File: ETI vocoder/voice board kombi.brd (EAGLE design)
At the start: 160 x 100 mm, 169 parts, among them IC1 TL072P, IC1. TL072P, IC2 TL072P, IC2. TL072P, IC3 TL081P, IC3. TL081P, IC4 TL081P, IC4. TL081P, IC5 TL072P, IC6 LM13600AN, IC7 TL072P, IC7. TL072P, Q1 BF244, Q1. BF244, Q2 BC214, Q2. BC214

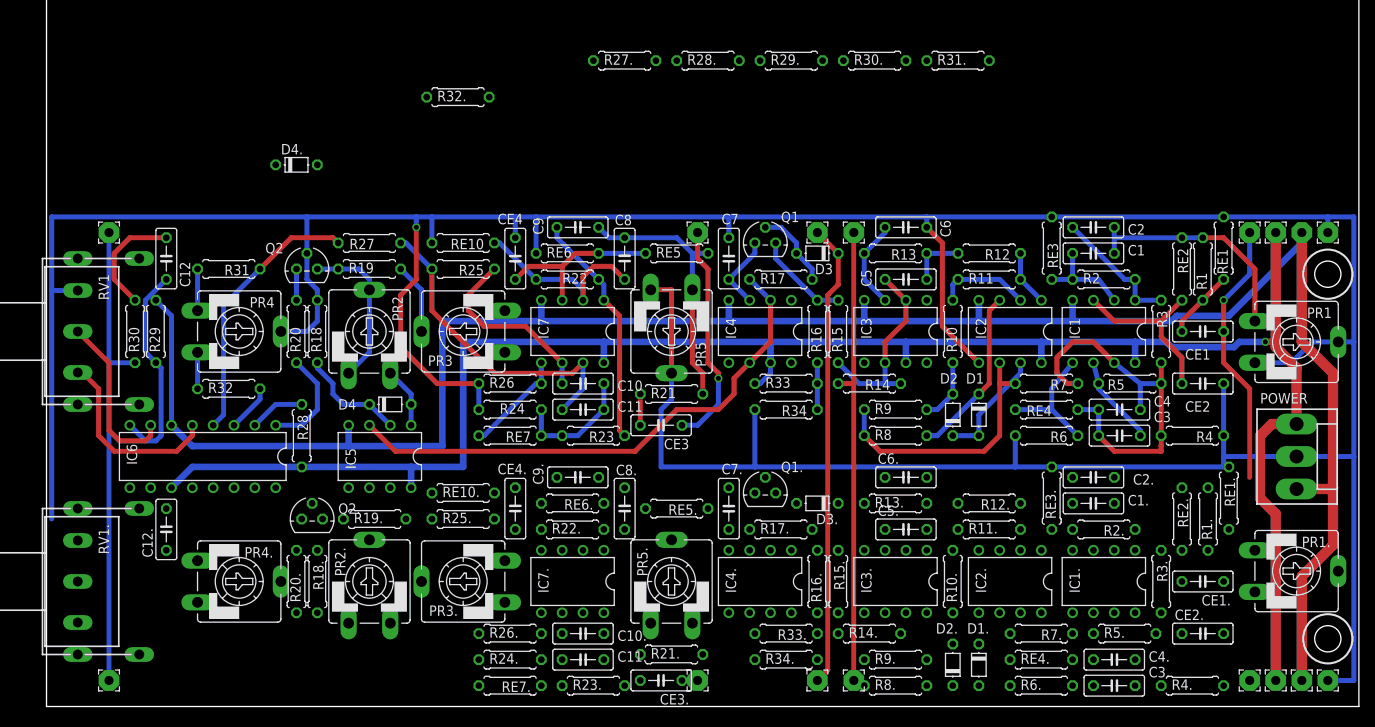
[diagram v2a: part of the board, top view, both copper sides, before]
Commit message: All airwires traced
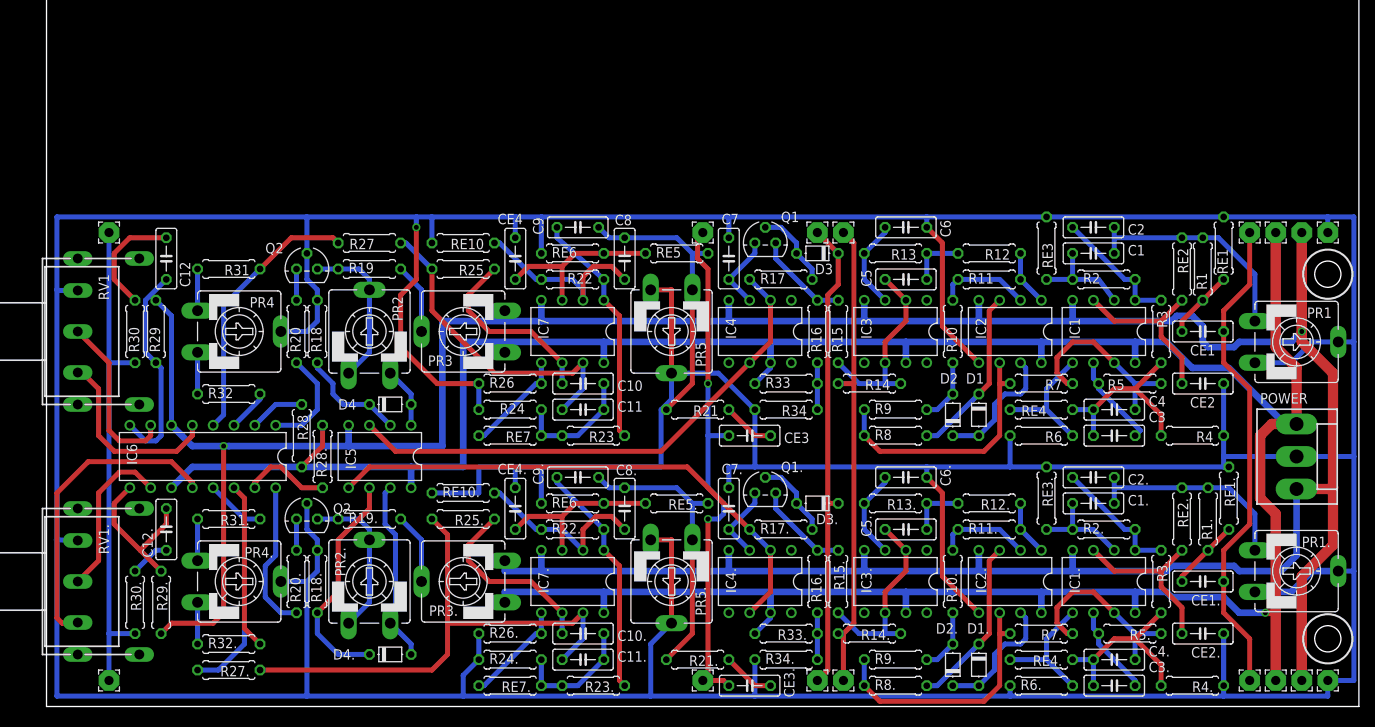
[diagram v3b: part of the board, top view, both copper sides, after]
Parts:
- moved R30. 111.8 mm to (10.8, 12.7), turned to 270 degrees
- moved R31. 105.0 mm to (22.2, 22.9), turned to 180 degrees
- moved R29. 101.3 mm to (14.0, 12.7), turned to 270 degrees
- moved R27. 88.6 mm to (22.2, 4.45), turned to 180 degrees
- moved R32. 72.3 mm to (22.2, 7.62)
- moved R28. 67.4 mm to (33.7, 30.5), turned to 90 degrees
- moved D4. 60.8 mm to (41.9, 6.35)
- moved CE3 10.9 mm to (85.7, 33.0), turned to 0 degrees
- moved CE3. 10.8 mm to (85.7, 2.54), turned to 0 degrees
- moved R21 3.70 mm to (79.4, 36.2), turned to 180 degrees
- moved R21. 3.24 mm to (79.4, 5.71), turned to 180 degrees
- moved PAD7 1.27 mm to (97.2, 57.8)
- moved PAD8 1.27 mm to (97.2, 3.17)
- moved R5. 0.64 mm to (132.1, 8.89), turned to 180 degrees
- moved PAD3 0.64 mm to (80.0, 57.8)
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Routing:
- net GND: track 486.7 -> 826.8 mm
- net -12V: track 254.1 -> 401.5 mm, vias 0 -> 2
- net +12V: track 231.7 -> 356.0 mm
- net N$66: track 0.00 -> 65.4 mm
- net N$77: track 0.00 -> 64.8 mm
- net N$92: track 0.00 -> 37.9 mm
- net EXITATION_IN: track 27.5 -> 64.0 mm, vias 1 -> 2
- net N$73: track 0.00 -> 35.0 mm
- net N$54: track 0.00 -> 31.4 mm
- net N$81: track 0.00 -> 29.6 mm
- net N$76: track 0.00 -> 28.8 mm
- net N$67: track 0.00 -> 27.8 mm
- net SPEECH_IN: track 32.5 -> 59.9 mm, vias 1 -> 0
- net N$48: track 0.00 -> 26.1 mm
- net N$61: track 0.00 -> 23.5 mm
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
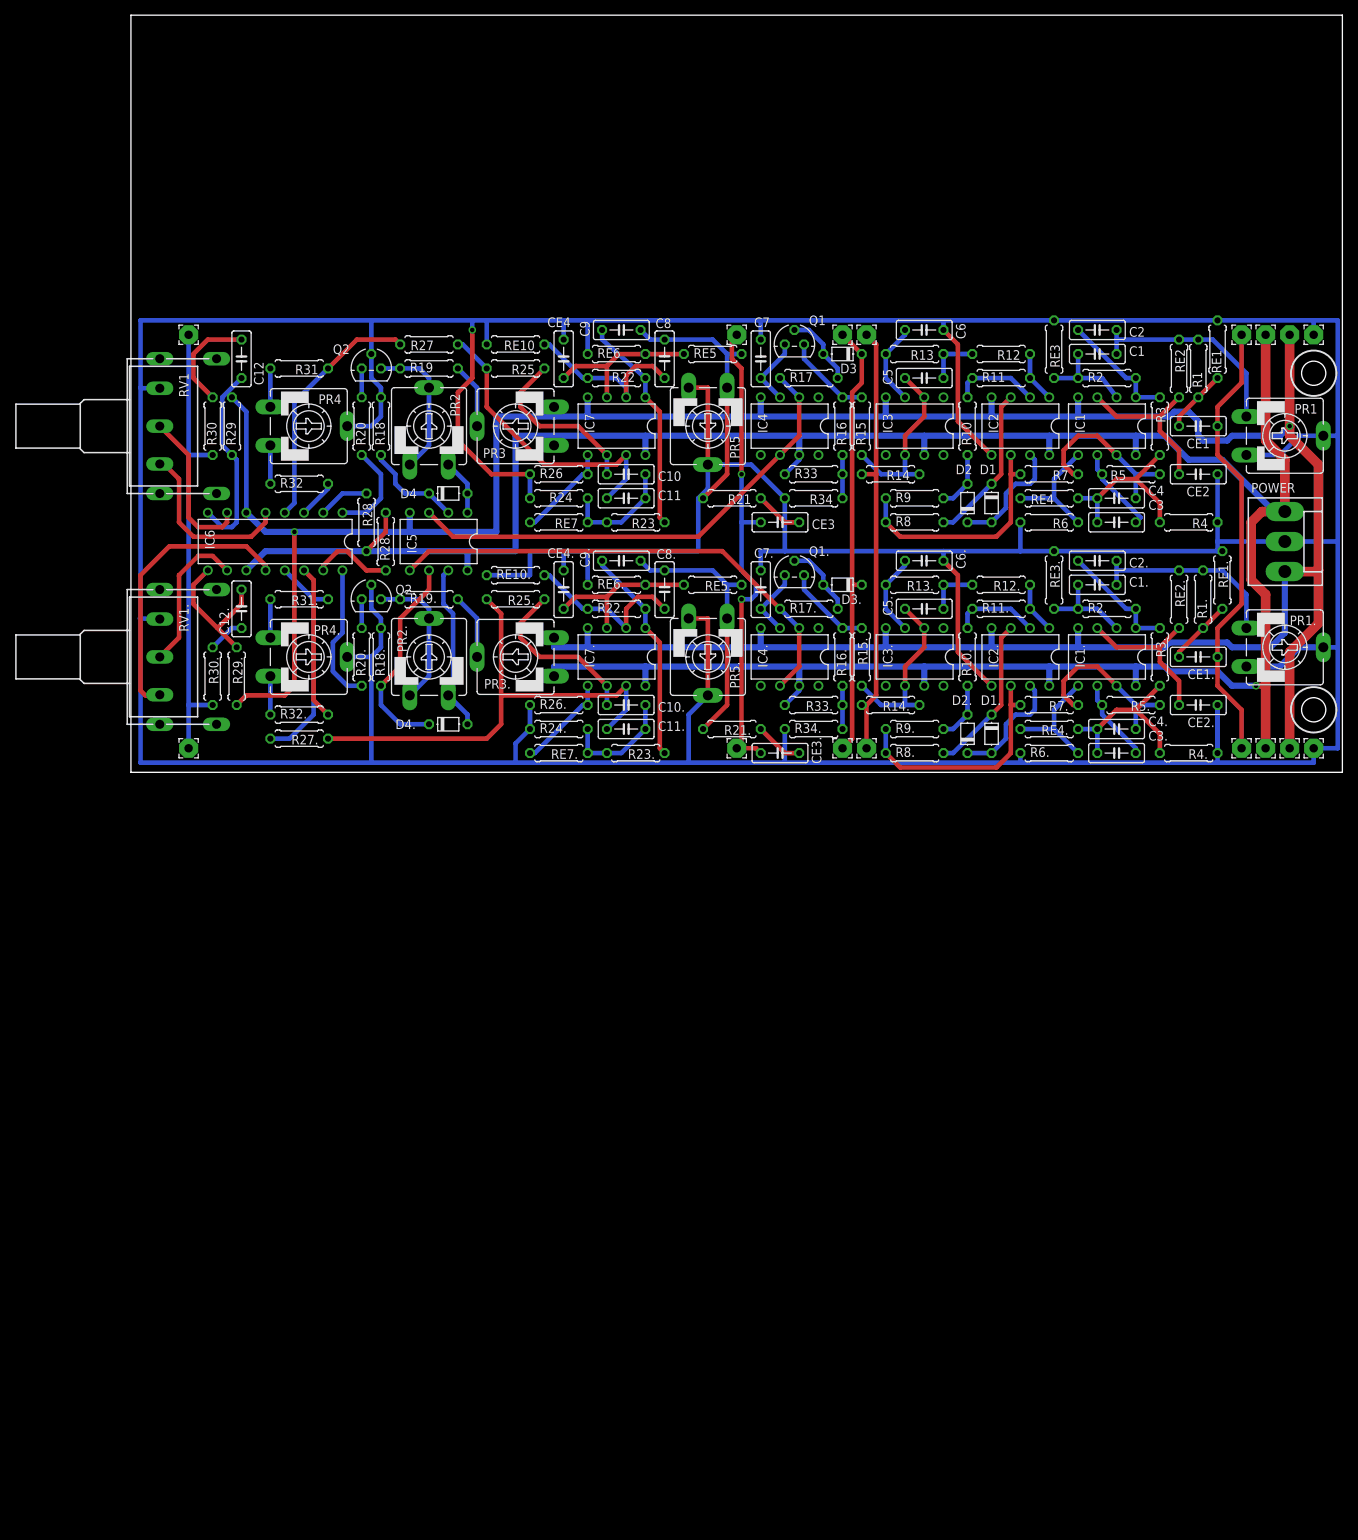
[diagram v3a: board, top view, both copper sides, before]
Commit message: All airwires traced
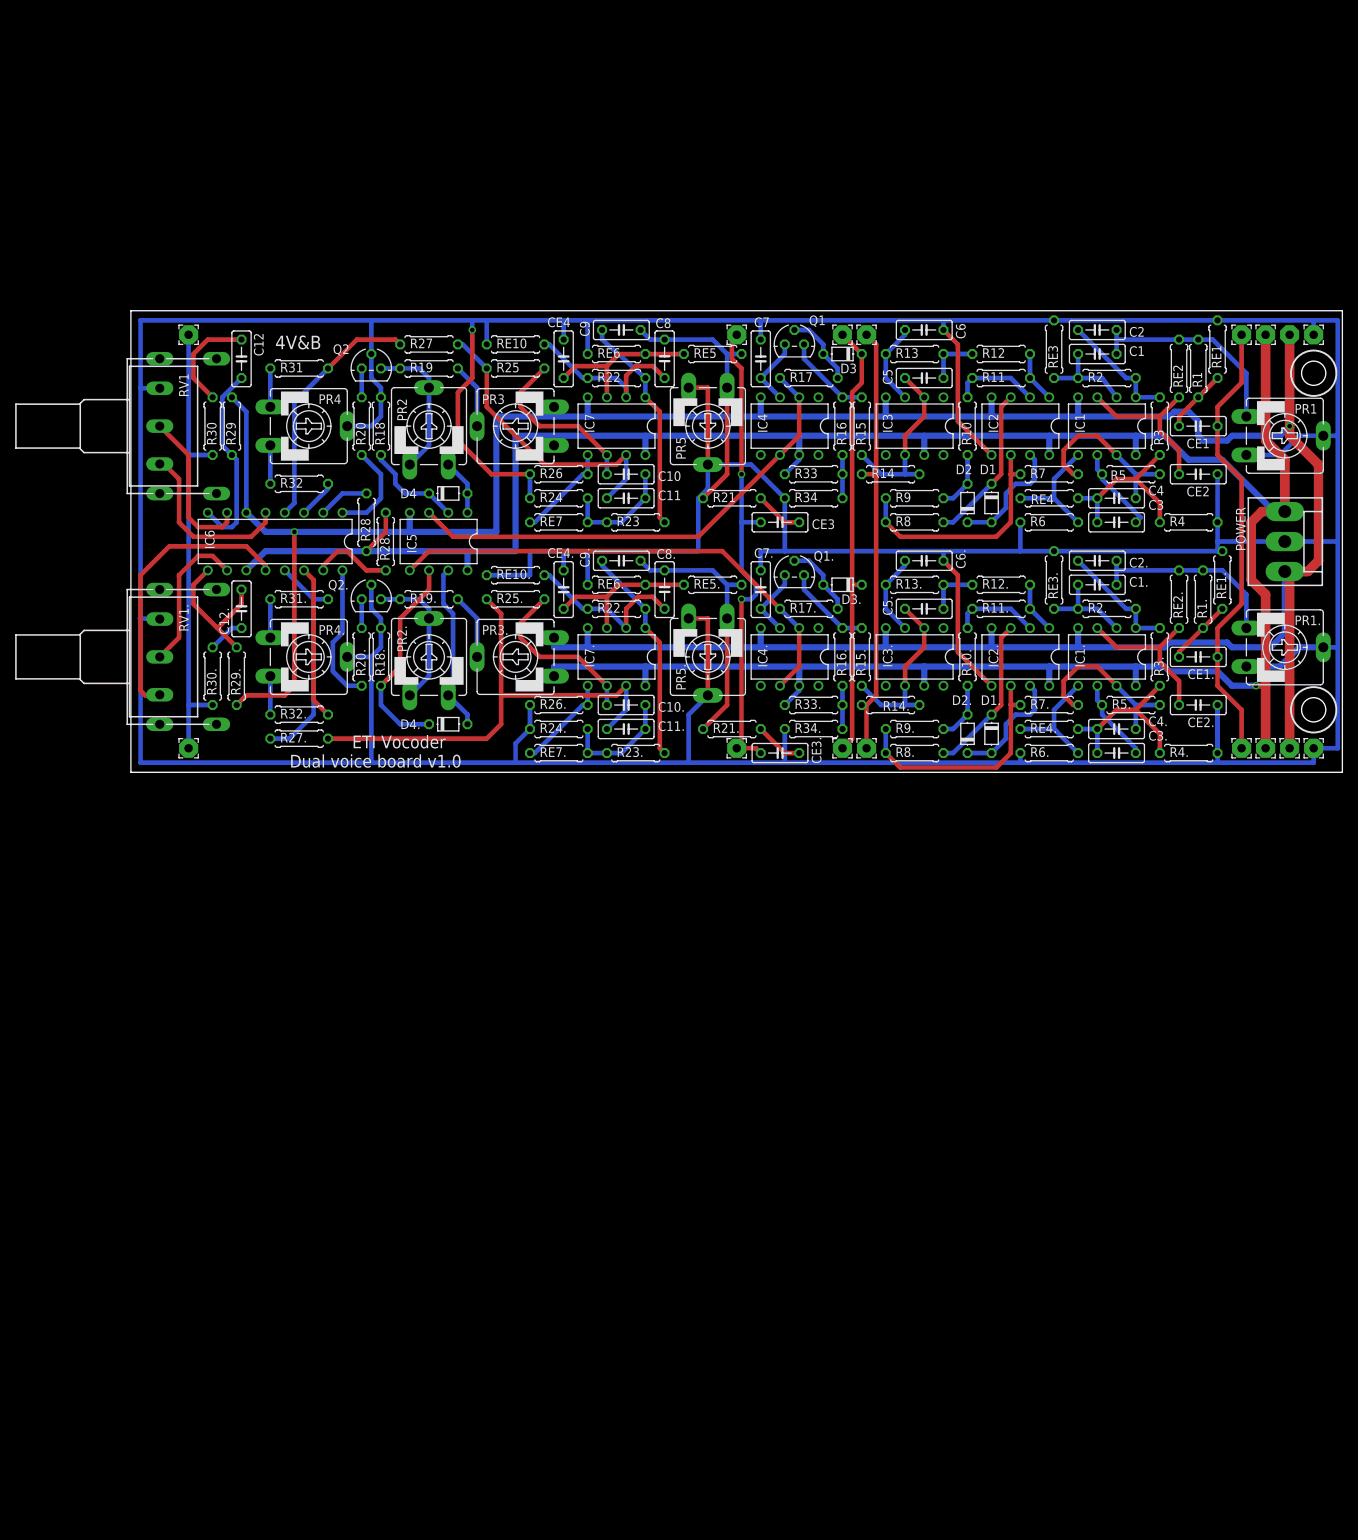
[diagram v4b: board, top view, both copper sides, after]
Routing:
- net -12V: track 401.5 -> 399.2 mm
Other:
- board size 160 x 100 mm -> 160 x 61 mm
- board text added: "+12v"
- board text added: "-12v"
- board text added: "4V&B"
- board text added: "Dual voice board v1.0"
- board text added: "ETI Vocoder"
- board text added: "Excit"
- board text added: "Gnd"
- board text added: "Slew"
- board text added: "Speech"
- board text added: "V/UV"

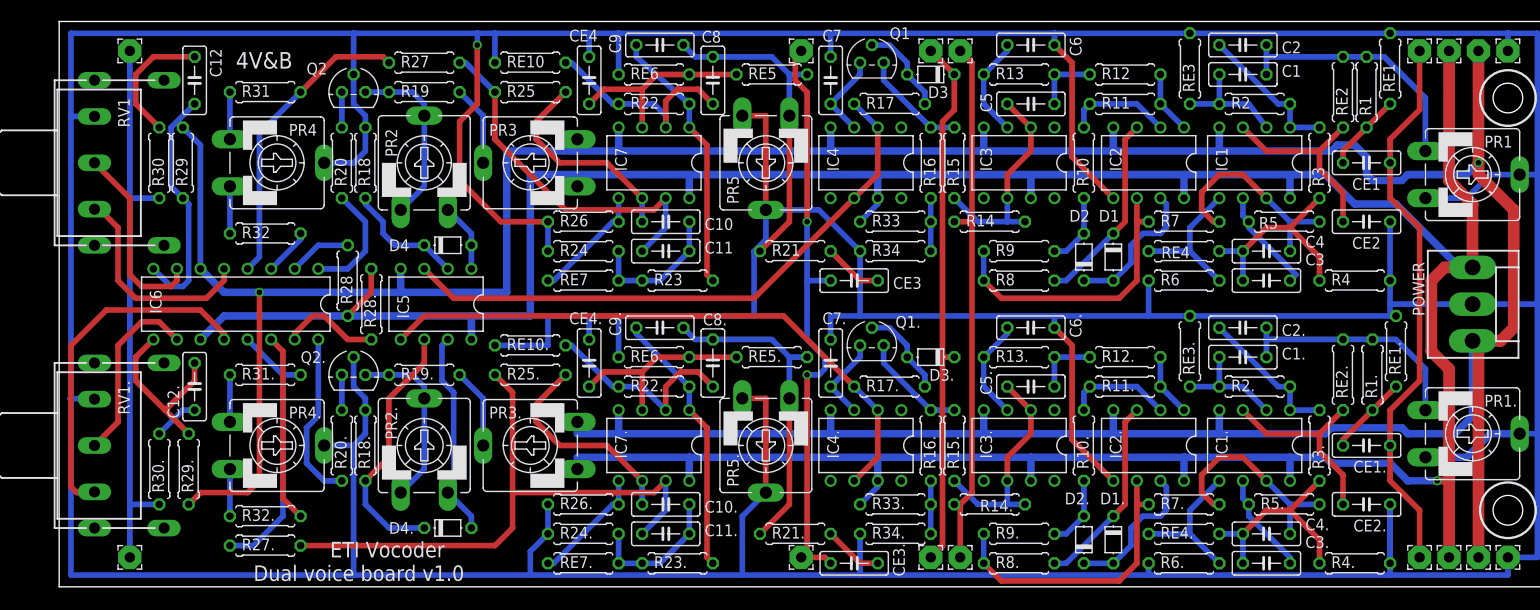
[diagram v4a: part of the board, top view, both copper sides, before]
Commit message: Checked and fixed Q2, still need to check cap footprints and shrink board
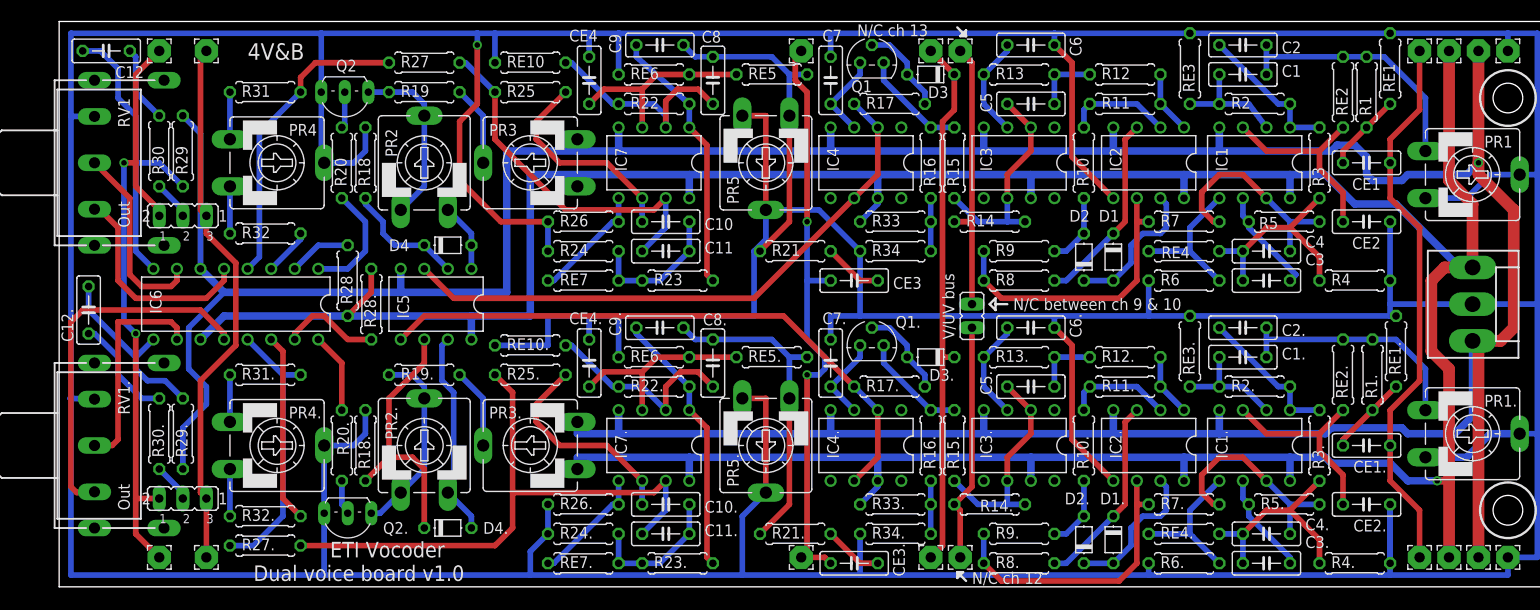
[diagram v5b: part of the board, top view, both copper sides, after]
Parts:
- added J1, J2: (no value), jumper:JP2
- added JP1: (no value), jumper:JP1
- added PAD17, PAD18: WIREPAD2,54/1,1, wirepad:2,54/1,1
- Q1, Q1.: value BF244 -> BF244C
- Q2, Q2.: value BC214 -> BC212L; device transistor-pnp:TO92 -> transistor-neu-to92:TO92-ECB
- moved Q2. 14.9 mm to (31.1, 7.94), turned to 180 degrees
- moved C12. 14.1 mm to (3.17, 29.8)
- moved C12 10.0 mm to (5.08, 57.8), turned to 180 degrees
- moved PAD1 8.25 mm to (15.9, 57.8)
- moved PAD2 8.25 mm to (15.9, 3.17)
- moved R29. 3.86 mm to (13.3, 16.5)
- moved R30. 3.81 mm to (10.8, 16.5)
- moved R29 1.27 mm to (13.3, 47.0)
- moved R30 1.27 mm to (10.8, 47.0)
- moved Q2 0.95 mm to (30.8, 53.3), turned to 180 degrees
- turned R20. to 270 degrees
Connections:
- new net OUT1: J1.3, J2.3, PAD1.1, PAD2.1
- new net OUT2: J1.1, J2.1, PAD17.1, PAD18.1
- new net OUTPUT_AMP_2: J2.2, R30..2
- new net VU_DETECTOR_2: JP1.2, PAD8.1, R14..2
- net GND: now also Q2..B, Q2.B; no longer Q2..2, Q2.2
- net N$23: now also Q2.E; no longer Q2.1
- net N$25: now also Q2.C; no longer Q2.3
- net N$69: now also Q2..E; no longer Q2..1
- net N$71: now also Q2..C; no longer Q2..3
- net OUTPUT_AMP: now also J1.2; no longer PAD1.1, PAD2.1, R30..2
- net VU_DETECTOR: now also JP1.1; no longer PAD8.1, R14..2
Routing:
- net OUT2: track 0.00 -> 67.8 mm, vias 0 -> 2
- net OUT1: track 0.00 -> 58.3 mm
- net OUTPUT_AMP: track 61.0 -> 4.23 mm
- net VU_DETECTOR: track 58.2 -> 29.7 mm
- net VU_DETECTOR_2: track 0.00 -> 25.8 mm
- net N$82: track 18.5 -> 8.67 mm
- net N$33: track 25.8 -> 33.9 mm
- net N$85: track 4.86 -> 11.6 mm
- net N$34: track 13.9 -> 8.30 mm
- net -12V: track 399.2 -> 394.7 mm, vias 2 -> 1
- net OUTPUT_AMP_2: track 0.00 -> 4.23 mm
- net N$83: track 20.0 -> 23.4 mm
- net GND: track 826.8 -> 823.9 mm
- net N$69: track 19.4 -> 20.9 mm
- net N$92: track 37.9 -> 39.3 mm
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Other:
- board text added: "1"
- board text added: "1 3 5 7 9 11 13"
- board text added: "1: Ch 1,2,4,6,8,10,12,14"
- board text added: "2"
- board text added: "2 4 6 8 10 12 14"
- board text added: "2: Ch 3,5,7,9,11,13"
- board text added: "Channel:"
- board text added: "Excit input"
- board text added: "N/C between ch 9 & 10"
- board text added: "N/C ch 12"
- board text added: "N/C ch 13"
- board text added: "Out"
- board text added: "Out 1"
- board text added: "Out 2"
- board text added: "Output buses:"
- board text added: "V/UV bus"
- board text removed: "Excit"
